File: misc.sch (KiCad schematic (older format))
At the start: 23 parts, among them CN8 POWER_INPUT, CN9 LED_CONNECTOR, SW1 POWER_SWITCH, SW2 RESET_SW, U10 NE555P, U11 74LS125, U9 74LS06

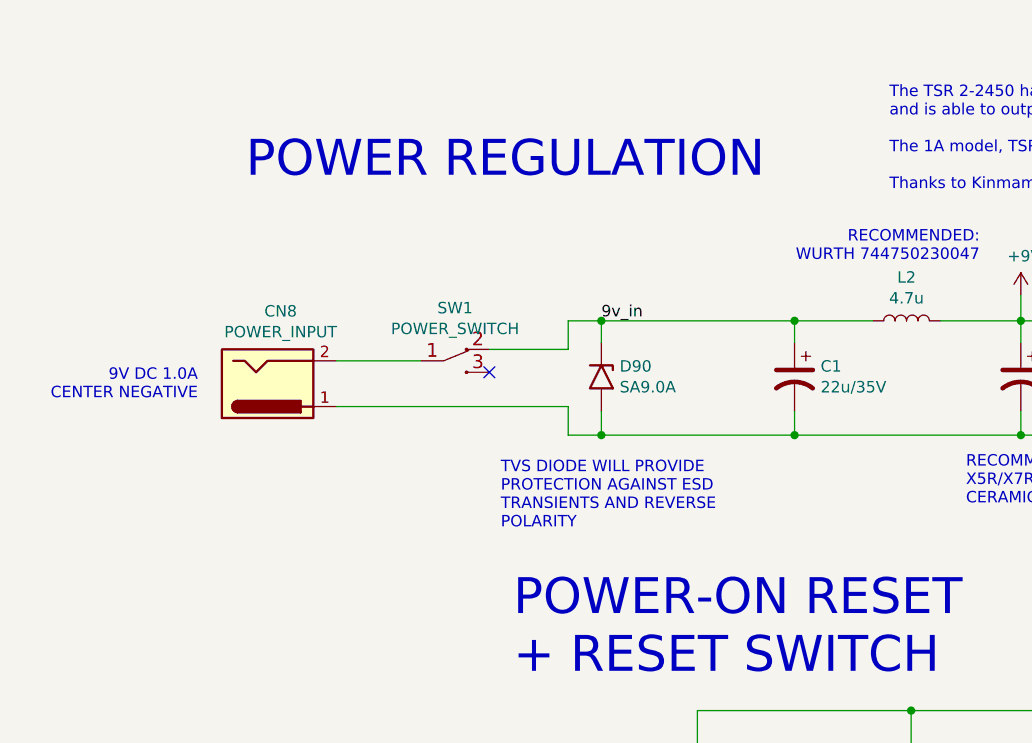
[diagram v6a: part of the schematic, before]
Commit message: Fix power switch
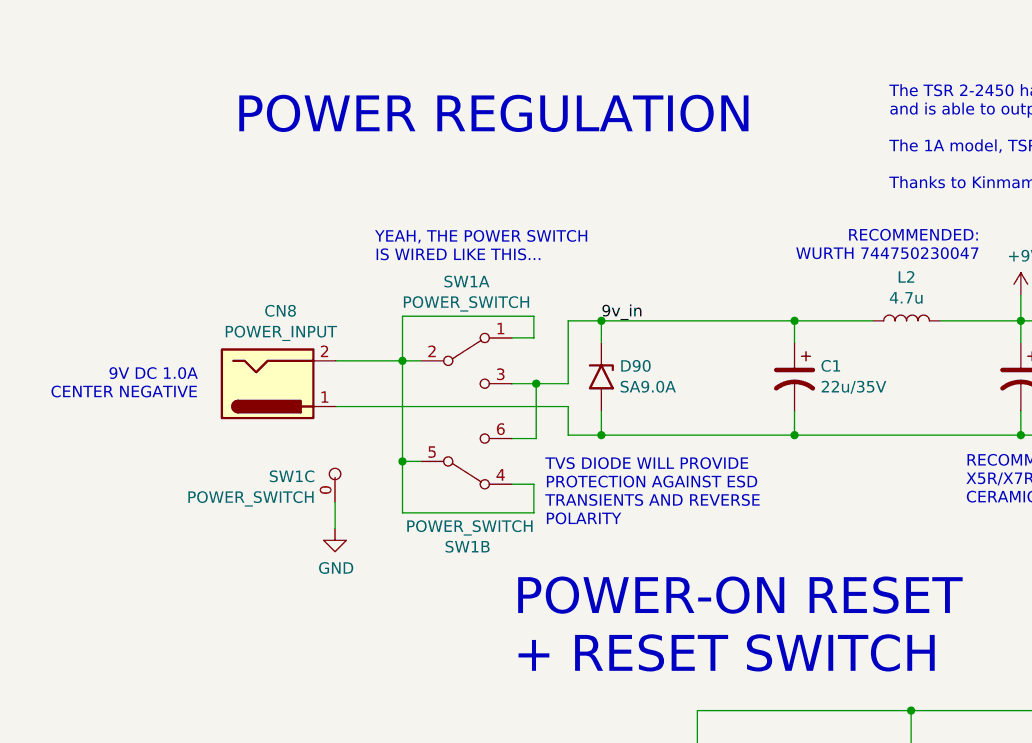
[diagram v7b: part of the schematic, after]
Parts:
- removed SW1: POWER_SWITCH, LittleSixteen:Switch-Rocker, symbol w_device:SW_SPDT
- added SW1: POWER_SWITCH, LittleSixteen:Switch-Rocker, symbol power_switch:SW_DPDT_x2
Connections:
- net 9v_in: now also SW1.3 (C), SW1.6 (C)
- net GND: now also SW1.0 (SH)
- net at CN8.2: now also SW1.1 (A), SW1.2 (B), SW1.4 (A), SW1.5 (B)
- no-connect marks 5 -> 4
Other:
- note added: "YEAH, THE POWER SWITCH\nIS WIRED LIKE THIS..."
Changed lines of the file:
@@
 Sheet 9 12
 Title "LittleSixteen"
-Date "2021-11-23"
+Date "2021-11-24"
 Rev "3git"
 Comp "SukkoPera"
@@
 NoConn ~ 10160 5960
 Wire Wire Line
-	3370 2090 3370 1965
-Wire Wire Line
 	3370 1965 3515 1965
 Wire Wire Line
@@
 	1    0    0    -1
 $EndComp
-Text Notes 1960 1355 0    157  ~ 0
+Text Notes 1910 1165 0    157  ~ 0
 POWER REGULATION
 Text Notes 4775 1400 0    50   ~ 0
@@
 Wire Wire Line
 	2355 2340 3370 2340
-$Comp
-L w_device:SW_SPDT SW1
-U 1 1 5ED32B7C
-P 2875 2140
-F 0 "SW1" H 2875 2371 50  0000 C CNN
-F 1 "POWER_SWITCH" H 2875 2280 50  0000 C CNN
-F 2 "LittleSixteen:Switch-Rocker" H 2875 2140 60  0001 C CNN
-F 3 "" H 2875 2140 60  0000 C CNN
-	1    2875 2140
-	1    0    0    -1
-$EndComp
-Wire Wire Line
-	2355 2140 2725 2140
-Wire Wire Line
-	3025 2090 3370 2090
-NoConn ~ 3025 2190
+Wire Wire Line
+	2355 2140 2645 2140
 $Comp
 L Device:CP1 C?
@@
 Wire Wire Line
 	3515 2465 4360 2465
-Text Notes 3075 2880 0    50   ~ 0
+Text Notes 3270 2870 0    50   ~ 0
 TVS DIODE WILL PROVIDE\nPROTECTION AGAINST ESD\nTRANSIENTS AND REVERSE\nPOLARITY
 Text Label 3515 1965 0    50   ~ 0
 9v_in
+$Comp
+L power_switch:SW_DPDT_x2 SW1
+U 1 1 62A43028
+P 2925 2140
+F 0 "SW1" H 2925 2485 50  0000 C CNN
+F 1 "POWER_SWITCH" H 2925 2395 50  0000 C CNN
+F 2 "LittleSixteen:Switch-Rocker" H 2925 2140 50  0001 C CNN
+F 3 "~" H 2925 2140 50  0001 C CNN
+	1    2925 2140
+	1    0    0    -1
+$EndComp
+$Comp
+L power_switch:SW_DPDT_x2 SW1
+U 2 1 62A43AA2
+P 2925 2580
+F 0 "SW1" H 2930 2955 50  0000 C CNN
+F 1 "POWER_SWITCH" H 2940 2865 50  0000 C CNN
+F 2 "LittleSixteen:Switch-Rocker" H 2925 2580 50  0001 C CNN
+F 3 "~" H 2925 2580 50  0001 C CNN
+	2    2925 2580
+	1    0    0    1
+$EndComp
+Wire Wire Line
+	3125 2240 3230 2240
+Wire Wire Line
+	3370 1965 3370 2240
+Wire Wire Line
+	2645 2140 2645 1945
+Wire Wire Line
+	2645 1945 3220 1945
+Wire Wire Line
+	3220 1945 3220 2040
+Wire Wire Line
+	3220 2040 3125 2040
+Connection ~ 2645 2140
+Wire Wire Line
+	2645 2140 2725 2140
+Wire Wire Line
+	2645 2140 2645 2580
+Wire Wire Line
+	2645 2580 2725 2580
+Wire Wire Line
+	2645 2580 2645 2805
+Wire Wire Line
+	2645 2805 3220 2805
+Wire Wire Line
+	3220 2805 3220 2680
+Wire Wire Line
+	3220 2680 3125 2680
+Connection ~ 2645 2580
+Wire Wire Line
+	3125 2480 3230 2480
+Wire Wire Line
+	3230 2480 3230 2240
+Connection ~ 3230 2240
+Wire Wire Line
+	3230 2240 3370 2240
+$Comp
+L power_switch:SW_DPDT_x2 SW1
+U 3 1 62A474EB
+P 2350 2685
+F 0 "SW1" H 2437 2723 50  0000 L CNN
+F 1 "POWER_SWITCH" H 2437 2632 50  0000 L CNN
+F 2 "LittleSixteen:Switch-Rocker" H 2350 2685 50  0001 C CNN
+F 3 "~" H 2350 2685 50  0001 C CNN
+	3    2350 2685
+	-1   0    0    -1
+$EndComp
+$Comp
+L power:GND #PWR0197
+U 1 1 62A6B46E
+P 2350 2875
+F 0 "#PWR0197" H 2350 2625 50  0001 C CNN
+F 1 "GND" H 2355 2702 50  0000 C CNN
+F 2 "" H 2350 2875 50  0001 C CNN
+F 3 "" H 2350 2875 50  0001 C CNN
+	1    2350 2875
+	1    0    0    -1
+$EndComp
+Wire Wire Line
+	2350 2760 2350 2875
+Text Notes 2525 1715 0    50   ~ 0
+YEAH, THE POWER SWITCH\nIS WIRED LIKE THIS...
 $EndSCHEMATC

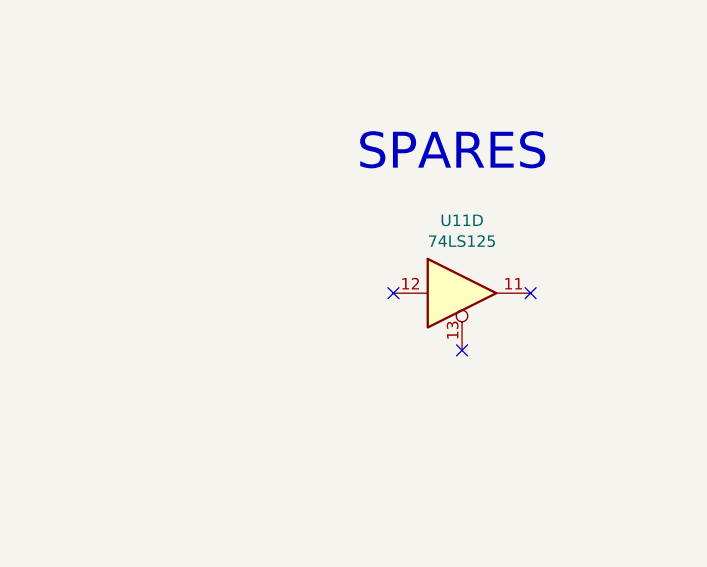
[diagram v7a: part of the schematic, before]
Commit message: Do not leave input pins of spare gate floating
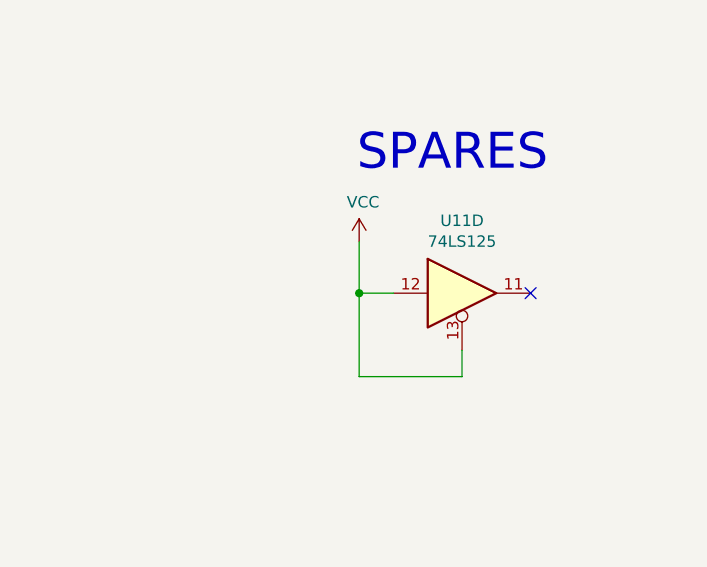
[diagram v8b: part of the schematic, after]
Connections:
- net VCC: now also U11.12, U11.13
- no-connect marks 4 -> 2
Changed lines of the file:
@@
 Text Notes 6865 5075 0    50   ~ 0
 This will be inverted\nseparately by U9B,\nno idea why
-$Comp
-L 74xx:74LS125 U?
-U 4 1 625FE5B6
-P 9860 5960
-AR Path="/5ECB474B/625FE5B6" Ref="U?"  Part="4"
-AR Path="/5EACE220/625FE5B6" Ref="U11"  Part="4"
-F 0 "U11" H 9860 6277 50  0000 C CNN
-F 1 "74LS125" H 9860 6186 50  0000 C CNN
-F 2 "Package_DIP:DIP-14_W7.62mm_Socket_LongPads" H 9860 5960 50  0001 C CNN
-F 3 "http://www.ti.com/lit/gpn/sn74LS125" H 9860 5960 50  0001 C CNN
-	4    9860 5960
-	1    0    0    -1
-$EndComp
-NoConn ~ 9560 5960
-NoConn ~ 9860 6210
 NoConn ~ 10160 5960
 Wire Wire Line
@@
 Text Notes 2525 1715 0    50   ~ 0
 YEAH, THE POWER SWITCH\nIS WIRED LIKE THIS...
+$Comp
+L 74xx:74LS125 U?
+U 4 1 625FE5B6
+P 9860 5960
+AR Path="/5ECB474B/625FE5B6" Ref="U?"  Part="4"
+AR Path="/5EACE220/625FE5B6" Ref="U11"  Part="4"
+F 0 "U11" H 9860 6277 50  0000 C CNN
+F 1 "74LS125" H 9860 6186 50  0000 C CNN
+F 2 "Package_DIP:DIP-14_W7.62mm_Socket_LongPads" H 9860 5960 50  0001 C CNN
+F 3 "http://www.ti.com/lit/gpn/sn74LS125" H 9860 5960 50  0001 C CNN
+	4    9860 5960
+	1    0    0    -1
+$EndComp
+Wire Wire Line
+	9560 5960 9410 5960
+Wire Wire Line
+	9410 5960 9410 5735
+Wire Wire Line
+	9410 5960 9410 6325
+Wire Wire Line
+	9410 6325 9860 6325
+Wire Wire Line
+	9860 6325 9860 6210
+Connection ~ 9410 5960
+$Comp
+L power:VCC #PWR0217
+U 1 1 62A8DCB8
+P 9410 5735
+F 0 "#PWR0217" H 9410 5585 50  0001 C CNN
+F 1 "VCC" H 9427 5908 50  0000 C CNN
+F 2 "" H 9410 5735 50  0001 C CNN
+F 3 "" H 9410 5735 50  0001 C CNN
+	1    9410 5735
+	1    0    0    -1
+$EndComp
 $EndSCHEMATC
